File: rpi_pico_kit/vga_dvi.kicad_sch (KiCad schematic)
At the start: 26 parts, among them J4 DB15_Female, J5 HDMI_A

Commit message: changed footprints from 0805 to 0603
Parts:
- C24, C25: footprint Capacitor_SMD:C_0805_2012Metric_Pad1.18x1.45mm_HandSolder -> Capacitor_SMD:C_0603_1608Metric_Pad1.08x0.95mm_HandSolder; Supplier Part URL https://www.digikey.cz/en/products/detail/kemet/C0805C104M3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 -> (none)
- R53, R54, R55, R56, R57, R58, R59, R60, R61, R62: footprint Resistor_SMD:R_0805_2012Metric_Pad1.20x1.40mm_HandSolder -> Resistor_SMD:R_0603_1608Metric_Pad0.98x0.95mm_HandSolder; Supplier Part URL https://www.digikey.cz/en/products/detail/yageo/RC0805FR-07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 -> (none)
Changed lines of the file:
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@@
       (effects (font (size 1.27 1.27)))
     )
-    (property "Footprint" "Capacitor_SMD:C_0805_2012Metric_Pad1.18x1.45mm_HandSolder" (id 2) (at 255.27 58.7248 0)
+    (property "Footprint" "Capacitor_SMD:C_0603_1608Metric_Pad1.08x0.95mm_HandSolder" (id 2) (at 255.27 58.7248 0)
       (effects (font (size 1.27 1.27)) hide)
     )
@@
       (effects (font (size 1.27 1.27)) hide)
     )
-    (property "Supplier Part URL" "https://www.digikey.cz/en/products/detail/kemet/C0805C104M3RAC7800/2211748" (id 6) (at 251.46 59.69 0)
+    (property "Supplier Part URL" "" (id 6) (at 251.46 59.69 0)
       (effects (font (size 1.27 1.27)) hide)
     )
@@
       (effects (font (size 1.27 1.27)))
     )
-    (property "Footprint" "Resistor_SMD:R_0805_2012Metric_Pad1.20x1.40mm_HandSolder" (id 2) (at 62.23 102.108 90)
+    (property "Footprint" "Resistor_SMD:R_0603_1608Metric_Pad0.98x0.95mm_HandSolder" (id 2) (at 62.23 102.108 90)
       (effects (font (size 1.27 1.27)) hide)
     )
@@
       (effects (font (size 1.27 1.27)) hide)
     )
-    (property "Supplier Part URL" "https://www.digikey.cz/en/products/detail/yageo/RC0805FR-07470RL/727976" (id 5) (at 62.23 100.33 0)
+    (property "Supplier Part URL" "" (id 5) (at 62.23 100.33 0)
       (effects (font (size 1.27 1.27)) hide)
     )
@@
       (effects (font (size 1.27 1.27)))
     )
-    (property "Footprint" "Resistor_SMD:R_0805_2012Metric_Pad1.20x1.40mm_HandSolder" (id 2) (at 62.23 97.028 90)
+    (property "Footprint" "Resistor_SMD:R_0603_1608Metric_Pad0.98x0.95mm_HandSolder" (id 2) (at 62.23 97.028 90)
       (effects (font (size 1.27 1.27)) hide)
     )
@@
       (effects (font (size 1.27 1.27)) hide)
     )
-    (property "Supplier Part URL" "https://www.digikey.cz/en/products/detail/yageo/RC0805FR-071KL/727444" (id 5) (at 62.23 95.25 0)
+    (property "Supplier Part URL" "" (id 5) (at 62.23 95.25 0)
       (effects (font (size 1.27 1.27)) hide)
     )
@@
       (effects (font (size 1.27 1.27)))
     )
-    (property "Footprint" "Resistor_SMD:R_0805_2012Metric_Pad1.20x1.40mm_HandSolder" (id 2) (at 133.35 97.028 90)
+    (property "Footprint" "Resistor_SMD:R_0603_1608Metric_Pad0.98x0.95mm_HandSolder" (id 2) (at 133.35 97.028 90)
       (effects (font (size 1.27 1.27)) hide)
     )
@@
       (effects (font (size 1.27 1.27)) hide)
     )
-    (property "Supplier Part URL" "https://www.digikey.cz/en/products/detail/yageo/RC0805FR-07100RL/727543" (id 5) (at 133.35 95.25 0)
+    (property "Supplier Part URL" "" (id 5) (at 133.35 95.25 0)
       (effects (font (size 1.27 1.27)) hide)
     )
@@
       (effects (font (size 1.27 1.27)))
     )
-    (property "Footprint" "Resistor_SMD:R_0805_2012Metric_Pad1.20x1.40mm_HandSolder" (id 2) (at 62.23 71.628 90)
+    (property "Footprint" "Resistor_SMD:R_0603_1608Metric_Pad0.98x0.95mm_HandSolder" (id 2) (at 62.23 71.628 90)
       (effects (font (size 1.27 1.27)) hide)
     )
@@
       (effects (font (size 1.27 1.27)) hide)
     )
-    (property "Supplier Part URL" "https://www.digikey.cz/en/products/detail/yageo/RC0805FR-072K2L/727676" (id 5) (at 62.23 69.85 0)
+    (property "Supplier Part URL" "" (id 5) (at 62.23 69.85 0)
       (effects (font (size 1.27 1.27)) hide)
     )
@@
       (effects (font (size 1.27 1.27)))
     )
-    (property "Footprint" "Resistor_SMD:R_0805_2012Metric_Pad1.20x1.40mm_HandSolder" (id 2) (at 62.23 112.268 90)
+    (property "Footprint" "Resistor_SMD:R_0603_1608Metric_Pad0.98x0.95mm_HandSolder" (id 2) (at 62.23 112.268 90)
       (effects (font (size 1.27 1.27)) hide)
     )
@@
       (effects (font (size 1.27 1.27)) hide)
     )
-    (property "Supplier Part URL" "https://www.digikey.cz/en/products/detail/yageo/RC0805FR-071KL/727444" (id 5) (at 62.23 110.49 0)
+    (property "Supplier Part URL" "" (id 5) (at 62.23 110.49 0)
       (effects (font (size 1.27 1.27)) hide)
     )
@@
       (effects (font (size 1.27 1.27)))
     )
-    (property "Footprint" "Resistor_SMD:R_0805_2012Metric_Pad1.20x1.40mm_HandSolder" (id 2) (at 62.23 81.788 90)
+    (property "Footprint" "Resistor_SMD:R_0603_1608Metric_Pad0.98x0.95mm_HandSolder" (id 2) (at 62.23 81.788 90)
       (effects (font (size 1.27 1.27)) hide)
     )
@@
       (effects (font (size 1.27 1.27)) hide)
     )
-    (property "Supplier Part URL" "https://www.digikey.cz/en/products/detail/yageo/RC0805FR-07470RL/727976" (id 5) (at 62.23 80.01 0)
+    (property "Supplier Part URL" "" (id 5) (at 62.23 80.01 0)
       (effects (font (size 1.27 1.27)) hide)
     )
@@
       (effects (font (size 1.27 1.27)) (justify right))
     )
-    (property "Footprint" "Capacitor_SMD:C_0805_2012Metric_Pad1.18x1.45mm_HandSolder" (id 2) (at 98.0948 100.33 0)
+    (property "Footprint" "Capacitor_SMD:C_0603_1608Metric_Pad1.08x0.95mm_HandSolder" (id 2) (at 98.0948 100.33 0)
       (effects (font (size 1.27 1.27)) hide)
     )
@@
       (effects (font (size 1.27 1.27)) hide)
     )
-    (property "Supplier Part URL" "https://www.digikey.cz/en/products/detail/kemet/C0805C104M3RAC7800/2211748" (id 6) (at 99.06 104.14 0)
+    (property "Supplier Part URL" "" (id 6) (at 99.06 104.14 0)
       (effects (font (size 1.27 1.27)) hide)
     )
@@
       (effects (font (size 1.27 1.27)))
     )
-    (property "Footprint" "Resistor_SMD:R_0805_2012Metric_Pad1.20x1.40mm_HandSolder" (id 2) (at 62.23 91.948 90)
+    (property "Footprint" "Resistor_SMD:R_0603_1608Metric_Pad0.98x0.95mm_HandSolder" (id 2) (at 62.23 91.948 90)
       (effects (font (size 1.27 1.27)) hide)
     )
@@
       (effects (font (size 1.27 1.27)) hide)
     )
-    (property "Supplier Part URL" "https://www.digikey.cz/en/products/detail/yageo/RC0805FR-072K2L/727676" (id 5) (at 62.23 90.17 0)
+    (property "Supplier Part URL" "" (id 5) (at 62.23 90.17 0)
       (effects (font (size 1.27 1.27)) hide)
     )
@@
       (effects (font (size 1.27 1.27)))
     )
-    (property "Footprint" "Resistor_SMD:R_0805_2012Metric_Pad1.20x1.40mm_HandSolder" (id 2) (at 62.23 76.708 90)
+    (property "Footprint" "Resistor_SMD:R_0603_1608Metric_Pad0.98x0.95mm_HandSolder" (id 2) (at 62.23 76.708 90)
       (effects (font (size 1.27 1.27)) hide)
     )
@@
       (effects (font (size 1.27 1.27)) hide)
     )
-    (property "Supplier Part URL" "https://www.digikey.cz/en/products/detail/yageo/RC0805FR-071KL/727444" (id 5) (at 62.23 74.93 0)
+    (property "Supplier Part URL" "" (id 5) (at 62.23 74.93 0)
       (effects (font (size 1.27 1.27)) hide)
     )
@@
       (effects (font (size 1.27 1.27)))
     )
-    (property "Footprint" "Resistor_SMD:R_0805_2012Metric_Pad1.20x1.40mm_HandSolder" (id 2) (at 133.35 91.948 90)
+    (property "Footprint" "Resistor_SMD:R_0603_1608Metric_Pad0.98x0.95mm_HandSolder" (id 2) (at 133.35 91.948 90)
       (effects (font (size 1.27 1.27)) hide)
     )
@@
       (effects (font (size 1.27 1.27)) hide)
     )
-    (property "Supplier Part URL" "https://www.digikey.cz/en/products/detail/yageo/RC0805FR-07100RL/727543" (id 5) (at 133.35 90.17 0)
+    (property "Supplier Part URL" "" (id 5) (at 133.35 90.17 0)
       (effects (font (size 1.27 1.27)) hide)
     )
@@
       (effects (font (size 1.27 1.27)))
     )
-    (property "Footprint" "Resistor_SMD:R_0805_2012Metric_Pad1.20x1.40mm_HandSolder" (id 2) (at 62.23 117.348 90)
+    (property "Footprint" "Resistor_SMD:R_0603_1608Metric_Pad0.98x0.95mm_HandSolder" (id 2) (at 62.23 117.348 90)
       (effects (font (size 1.27 1.27)) hide)
     )
@@
       (effects (font (size 1.27 1.27)) hide)
     )
-    (property "Supplier Part URL" "https://www.digikey.cz/en/products/detail/yageo/RC0805FR-07390RL/727902" (id 6) (at 62.23 115.57 0)
-      (effects (font (size 1.27 1.27)) hide)
-    )
+    (property "Supplier Part URL" "" (id 6) (at 62.23 115.57 0)
+      (effects (font (size 1.27 1.27)) hide)
+    )

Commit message: pcb changes
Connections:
- net CLK+: now also RN2.7 (R2.2); no longer RN2.6 (R3.2)
- net CLK-: now also RN2.8 (R1.2); no longer RN2.5 (R4.2)
- net D0+: now also RN2.5 (R4.2); no longer RN2.8 (R1.2)
- net D0-: now also RN2.6 (R3.2); no longer RN2.7 (R2.2)
- net D1+: now also RN1.7 (R2.2); no longer RN1.6 (R3.2)
- net D1-: now also RN1.8 (R1.2); no longer RN1.5 (R4.2)
- net D2+: now also RN1.5 (R4.2); no longer RN1.8 (R1.2)
- net D2-: now also RN1.6 (R3.2); no longer RN1.7 (R2.2)
- net HSYNC: now also JP17.1 (A); no longer JP17.2 (B)
- net VSYNC: now also JP18.1 (A); no longer JP18.2 (B)
- net at R61.2: now also J4.13; no longer JP17.1 (A)
- net at J5.12 (CK-): now also RN2.1 (R1.1); no longer RN2.4 (R4.1)
- net at R62.1: now also JP18.2 (B); no longer J4.14
- net at R62.2: now also J4.14; no longer JP18.1 (A)
- net at J5.3 (D2-): now also RN1.3 (R3.1); no longer RN1.2 (R2.1)
- net at R61.1: now also JP17.2 (B); no longer J4.13
- net at J5.10 (CK+): now also RN2.2 (R2.1); no longer RN2.3 (R3.1)
- net at J5.1 (D2+): now also RN1.4 (R4.1); no longer RN1.1 (R1.1)
- net at J5.4 (D1+): now also RN1.2 (R2.1); no longer RN1.3 (R3.1)
- net at J5.6 (D1-): now also RN1.1 (R1.1); no longer RN1.4 (R4.1)
- net at J5.7 (D0+): now also RN2.4 (R4.1); no longer RN2.1 (R1.1)
- net at J5.9 (D0-): now also RN2.3 (R3.1); no longer RN2.2 (R2.1)
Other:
- moved on the sheet: R61, R62

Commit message: changed footprints for resistor arrays
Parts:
- RN1, RN2: footprint Resistor_SMD:R_Array_Convex_4x1206 -> Resistor_SMD:R_Array_Convex_4x0603
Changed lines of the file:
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@@
       (effects (font (size 1.27 1.27)))
     )
-    (property "Footprint" "Resistor_SMD:R_Array_Convex_4x1206" (id 2) (at 218.44 92.202 90)
+    (property "Footprint" "Resistor_SMD:R_Array_Convex_4x0603" (id 2) (at 218.44 92.202 90)
       (effects (font (size 1.27 1.27)) hide)
     )
@@
       (effects (font (size 1.27 1.27)))
     )
-    (property "Footprint" "Resistor_SMD:R_Array_Convex_4x1206" (id 2) (at 218.44 76.962 90)
+    (property "Footprint" "Resistor_SMD:R_Array_Convex_4x0603" (id 2) (at 218.44 76.962 90)
       (effects (font (size 1.27 1.27)) hide)
     )
@@
       (effects (font (size 1.27 1.27)))
     )
-    (property "Footprint" "Resistor_SMD:R_Array_Convex_4x1206" (id 2) (at 218.44 89.662 90)
+    (property "Footprint" "Resistor_SMD:R_Array_Convex_4x0603" (id 2) (at 218.44 89.662 90)
       (effects (font (size 1.27 1.27)) hide)
     )
@@
       (effects (font (size 1.27 1.27)))
     )
-    (property "Footprint" "Resistor_SMD:R_Array_Convex_4x1206" (id 2) (at 218.44 87.122 90)
+    (property "Footprint" "Resistor_SMD:R_Array_Convex_4x0603" (id 2) (at 218.44 87.122 90)
       (effects (font (size 1.27 1.27)) hide)
     )
@@
       (effects (font (size 1.27 1.27)))
     )
-    (property "Footprint" "Resistor_SMD:R_Array_Convex_4x1206" (id 2) (at 218.44 79.502 90)
+    (property "Footprint" "Resistor_SMD:R_Array_Convex_4x0603" (id 2) (at 218.44 79.502 90)
       (effects (font (size 1.27 1.27)) hide)
     )
@@
       (effects (font (size 1.27 1.27)))
     )
-    (property "Footprint" "Resistor_SMD:R_Array_Convex_4x1206" (id 2) (at 218.44 74.422 90)
+    (property "Footprint" "Resistor_SMD:R_Array_Convex_4x0603" (id 2) (at 218.44 74.422 90)
       (effects (font (size 1.27 1.27)) hide)
     )
@@
       (effects (font (size 1.27 1.27)))
     )
-    (property "Footprint" "Resistor_SMD:R_Array_Convex_4x1206" (id 2) (at 218.44 84.582 90)
+    (property "Footprint" "Resistor_SMD:R_Array_Convex_4x0603" (id 2) (at 218.44 84.582 90)
       (effects (font (size 1.27 1.27)) hide)
     )
@@
       (effects (font (size 1.27 1.27)))
     )
-    (property "Footprint" "Resistor_SMD:R_Array_Convex_4x1206" (id 2) (at 218.44 82.042 90)
-      (effects (font (size 1.27 1.27)) hide)
-    )
+    (property "Footprint" "Resistor_SMD:R_Array_Convex_4x0603" (id 2) (at 218.44 82.042 90)
+      (effects (font (size 1.27 1.27)) hide)
+    )

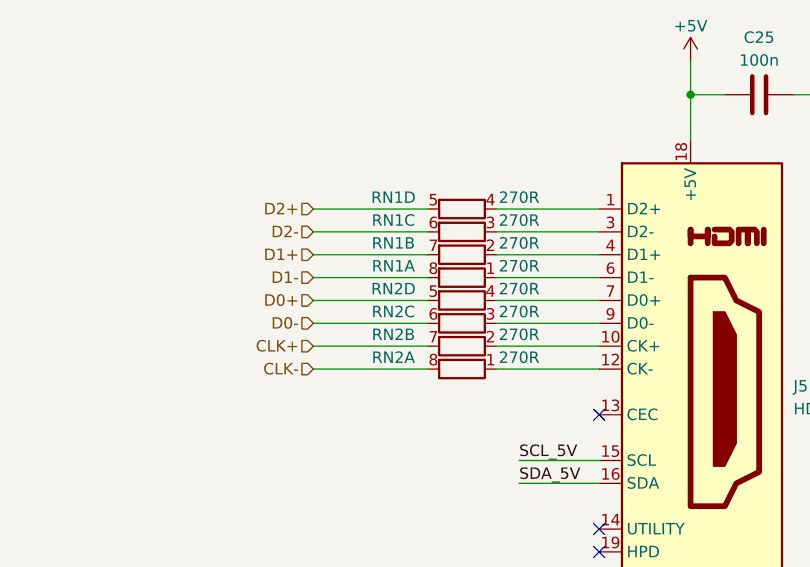
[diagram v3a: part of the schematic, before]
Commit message: added names to differential pairs
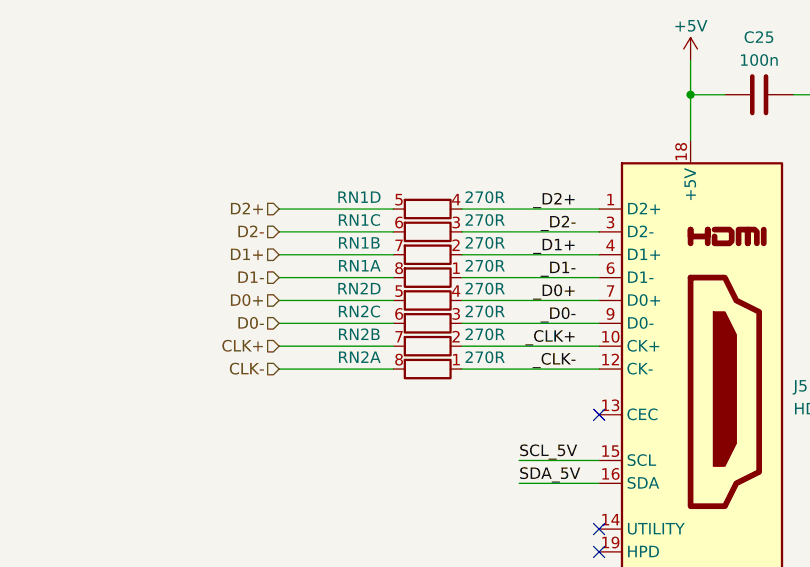
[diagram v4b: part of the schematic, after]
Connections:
- net _CLK-: now reaches J5.12 (CK-), RN2.1 (R1.1)
- net _D2-: now reaches J5.3 (D2-), RN1.3 (R3.1)
- net _CLK+: now reaches J5.10 (CK+), RN2.2 (R2.1)
- net _D2+: now reaches J5.1 (D2+), RN1.4 (R4.1)
- net _D1+: now reaches J5.4 (D1+), RN1.2 (R2.1)
- net _D1-: now reaches J5.6 (D1-), RN1.1 (R1.1)
- net _D0+: now reaches J5.7 (D0+), RN2.4 (R4.1)
- net _D0-: now reaches J5.9 (D0-), RN2.3 (R3.1)
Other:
- moved on the sheet: RN1A, RN1B, RN1C, RN1D, RN2A, RN2B, RN2C, RN2D

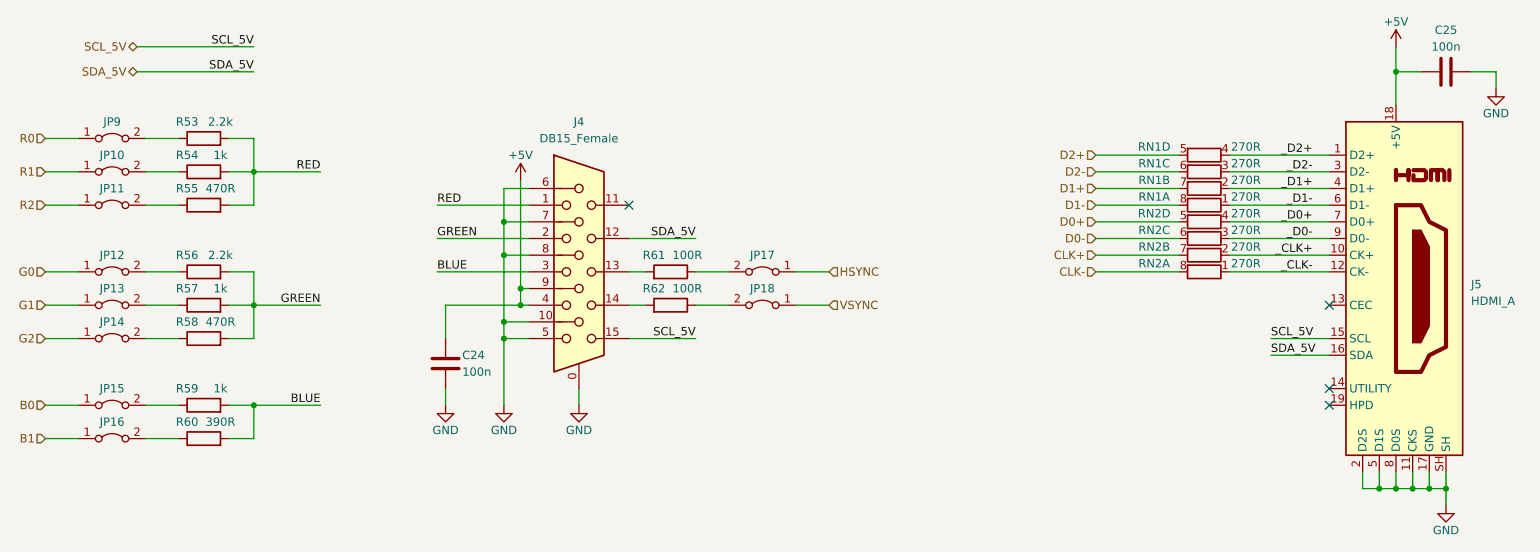
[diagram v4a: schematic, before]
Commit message: added nets to vga class
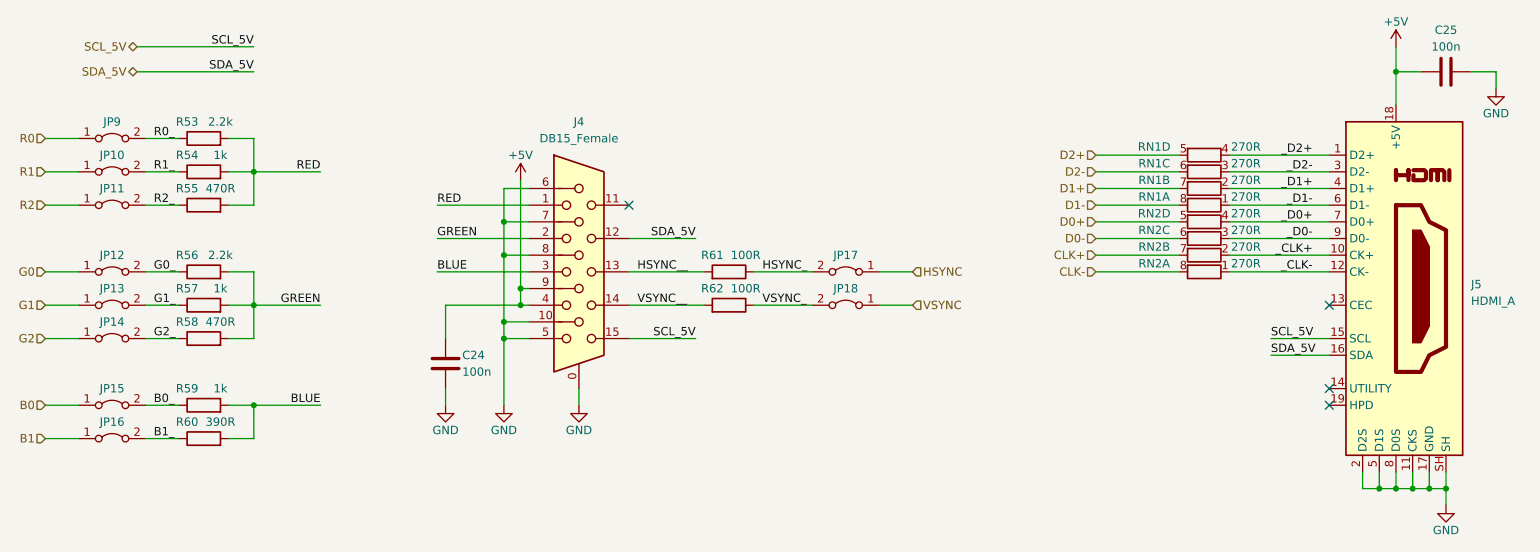
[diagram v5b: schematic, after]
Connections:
- net HSYNC_: now reaches JP17.2 (B), R61.1
- net G2_: now reaches JP14.2 (B), R58.1
- net G1_: now reaches JP13.2 (B), R57.1
- net VSYNC_: now reaches JP18.2 (B), R62.1
- net VSYNC__: now reaches J4.14, R62.2
- net R0_: now reaches JP9.2 (B), R53.1
- net HSYNC__: now reaches J4.13, R61.2
- net B1_: now reaches JP16.2 (B), R60.1
- net B0_: now reaches JP15.2 (B), R59.1
- net R2_: now reaches JP11.2 (B), R55.1
- net G0_: now reaches JP12.2 (B), R56.1
- net R1_: now reaches JP10.2 (B), R54.1
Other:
- moved on the sheet: JP17, JP18, R61, R62

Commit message: schematic cleared annotation
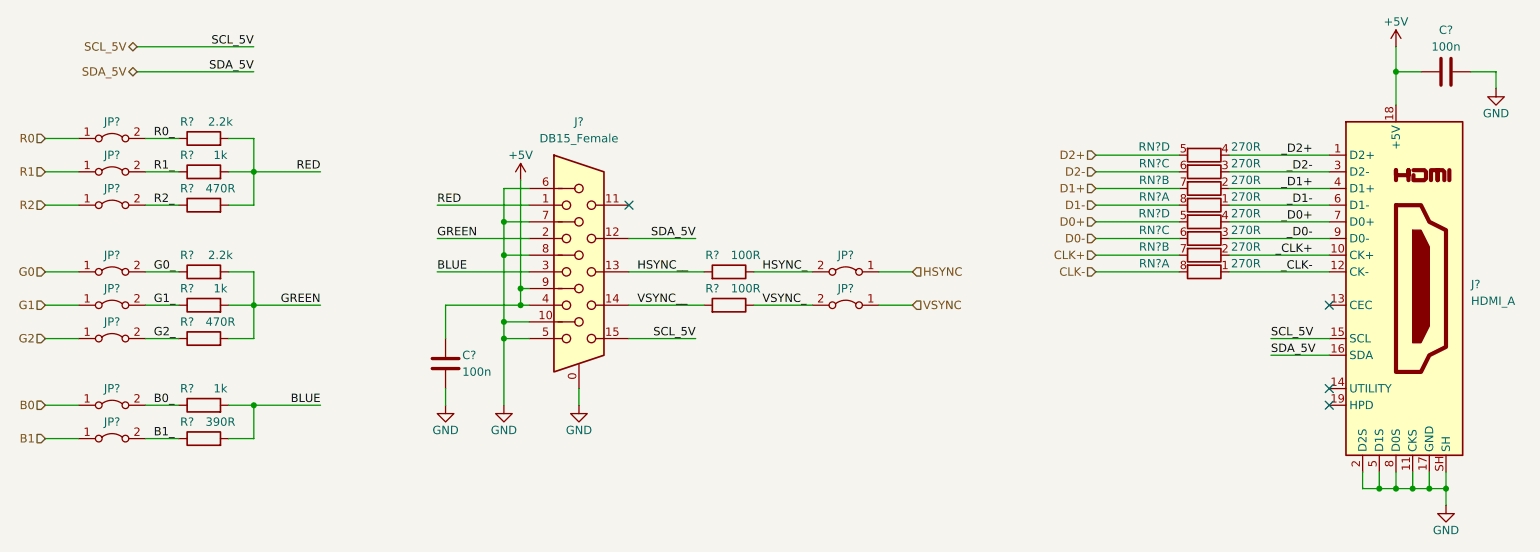
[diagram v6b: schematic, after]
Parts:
- renumbered C25 to C?, C24 to C?, J4 to J?, J5 to J?, JP17 to JP?, JP16 to JP?, JP13 to JP?, JP14 to JP?, JP11 to JP?, JP9 to JP?, JP18 to JP?, JP10 to JP?, JP15 to JP?, JP12 to JP?, R58 to R?, R57 to R?, R62 to R?, R53 to R?, R59 to R?, R55 to R?, R56 to R?, R54 to R?, R61 to R?, R60 to R?, RN2 to RN?, RN1 to RN?
